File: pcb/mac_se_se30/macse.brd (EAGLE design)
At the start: 52 x 24 mm, 8 parts, among them J1 ATX24RH

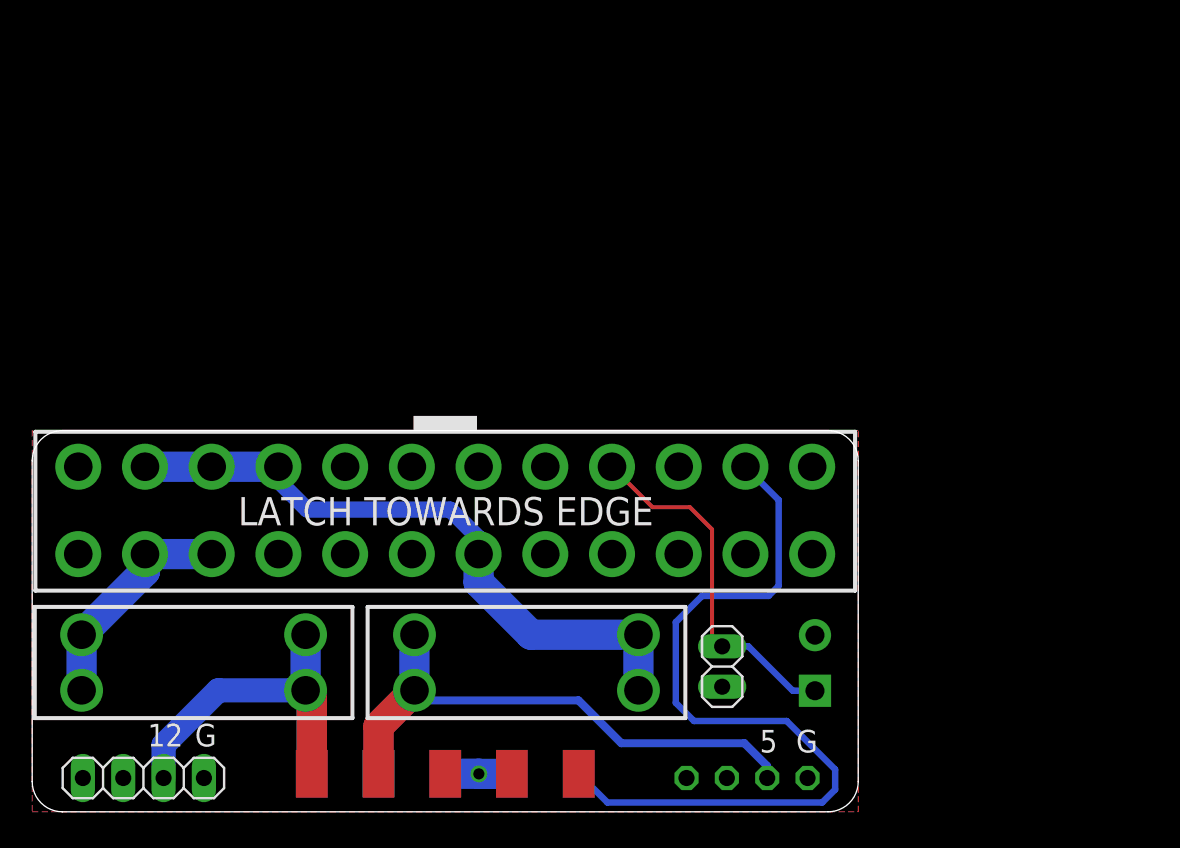
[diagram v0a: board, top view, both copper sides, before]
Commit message: updating mac SE atx adaptor
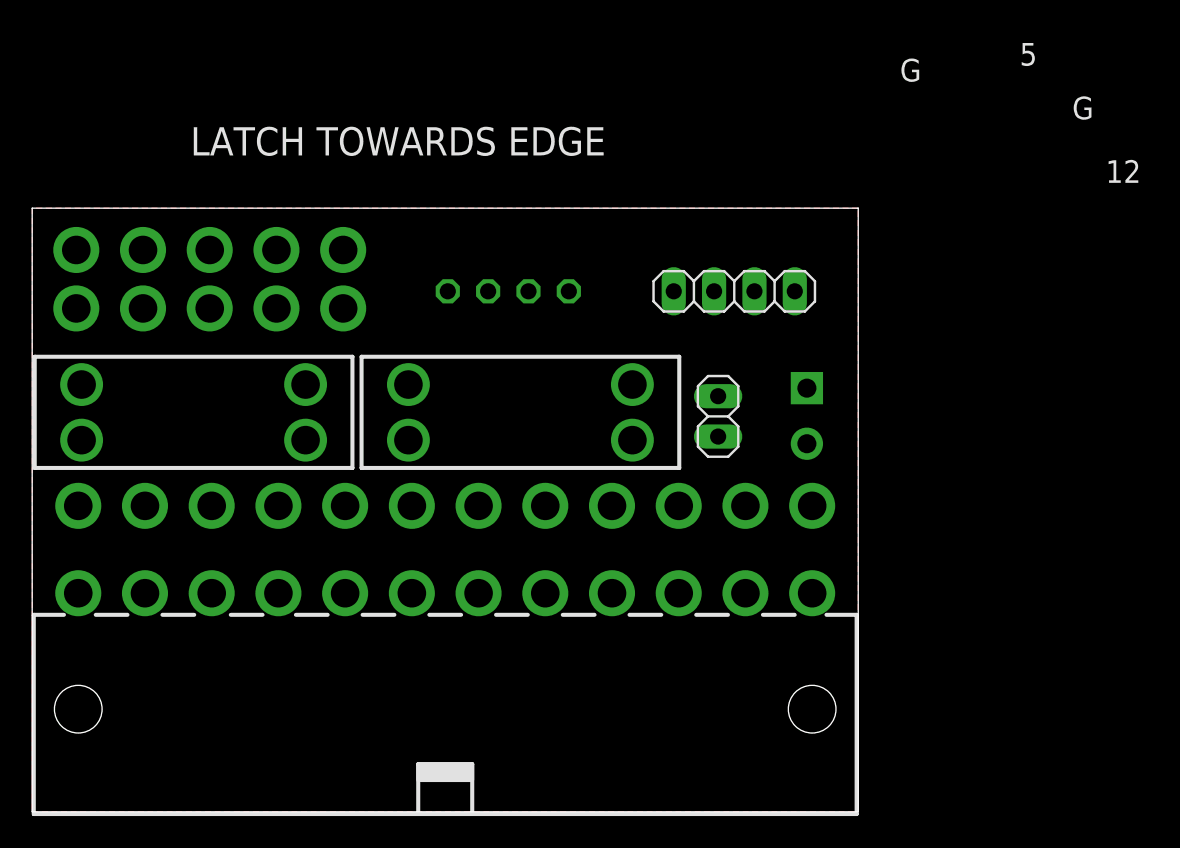
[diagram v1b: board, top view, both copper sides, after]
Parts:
- removed J1: ATX24RH, atx4vc:ATX24_STRAIGHT
- added J2: ATX24RH, SparkFun-Connectors:ATX24_RIGHT_ANGLE
- U$1: device atx4vc:MACSE_10P -> atx4vc:MACSE_10P_STRAIGHT
- moved JP1 48.2 mm to (44.2, 32.8), turned to 180 degrees
- moved U$1 34.5 mm to (11.2, 33.5), flipped to the top, turned to 0 degrees
- moved JP4 34.1 mm to (32.5, 32.8)
- moved J7 19.1 mm to (48.8, 26.7), turned to 270 degrees
- moved U$8 15.8 mm to (30.7, 25.1), turned to 180 degrees
- moved JP2 15.8 mm to (43.2, 24.9), turned to 90 degrees
- moved U$2 15.7 mm to (10.2, 25.1), turned to 180 degrees
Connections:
- net +12V: now also U$1.10, U$1.5; no longer U$1.P$10, U$1.P$5
- net +5V: now also U$1.4, U$1.9; no longer U$1.P$4, U$1.P$9
- net -12V: now also J2.14, U$1.6; no longer J1.14, U$1.P$6
- net GND: now also J2.15, J2.17, J2.18, J2.19, J2.24, J2.3, J2.5, J2.7, U$1.1, U$1.2, U$1.3, U$1.7, U$1.8; no longer J1.15, J1.17, J1.18, J1.19, J1.24, J1.3, J1.5, J1.7, U$1.P$1, U$1.P$2, U$1.P$3, U$1.P$7, U$1.P$8
- net N$5: now also J2.16; no longer J1.16
- net N$6: now also J2.21, J2.22, J2.23, J2.6; no longer J1.21, J1.22, J1.23, J1.6
- net N$8: now also J2.10, J2.11; no longer J1.10, J1.11
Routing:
- net -12V: track 51.1 -> 0.00 mm
- net N$6: track 41.1 -> 0.00 mm
- net +5V: track 40.8 -> 0.00 mm
- net +12V: track 26.8 -> 0.00 mm
- net N$5: track 22.6 -> 0.00 mm
- net N$8: track 14.4 -> 0.00 mm
- net GND: track 4.21 -> 0.00 mm, vias 1 -> 0
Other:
- board size 52 x 24 mm -> 52 x 38 mm

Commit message: updated mac SE pcb
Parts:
- removed JP4: (no value), adafruit_changed:1X06
- added JP3: (no value), atx_power_control:1X04
- added TP1: PTR1PAD1-20Y, testpad:P1-20Y
- J2: device SparkFun-Connectors:ATX24_RIGHT_ANGLE -> macse:ATX24_RIGHT_ANGLE
- moved U$2 20.6 mm to (30.7, 24.9)
- moved U$8 20.6 mm to (10.2, 24.9), turned to 0 degrees
- moved JP1 1.02 mm to (44.2, 33.8)
- moved U$1 0.38 mm to (11.2, 33.1)
- moved JP2 0.25 mm to (42.9, 24.9)
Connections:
- net +5V: now also JP3.3; no longer JP4.3
- net GND: now also JP3.4, TP1.TP; no longer JP4.4
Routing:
- net N$8: track 0.00 -> 73.5 mm
- net +12V: track 0.00 -> 70.9 mm
- net N$6: track 0.00 -> 65.6 mm
- net -12V: track 0.00 -> 58.6 mm
- net +5V: track 0.00 -> 40.3 mm
- net N$5: track 0.00 -> 15.3 mm
- net GND: track 0.00 -> 10.9 mm
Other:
- outline, holes or cut-outs redrawn
- board text added: "FUSE 5A MAX"
- board text added: "GND"
- board text added: "NOTCH TOWARDS EDGE"
- board text added: "PT1 dekuNukem Nov 2022"
- board text added: "PWR SW"
- board text removed: "LATCH TOWARDS EDGE"
- board text removed: "PT0 dekuNukem Nov 2022"

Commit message: finishing touches
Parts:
- added C1, C2: (no value), capacitor-wima:C5B2.5
- moved JP3 2.29 mm to (27.7, 33.8)
- moved JP1 1.27 mm to (45.5, 33.8)
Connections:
- net +12V: now also C1.1, C2.1
- net GND: now also C1.2, C2.2
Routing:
- net +12V: track 70.9 -> 72.6 mm
- net +5V: track 40.3 -> 38.8 mm
- net -12V: track 58.6 -> 59.6 mm
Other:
- board text added: "+"

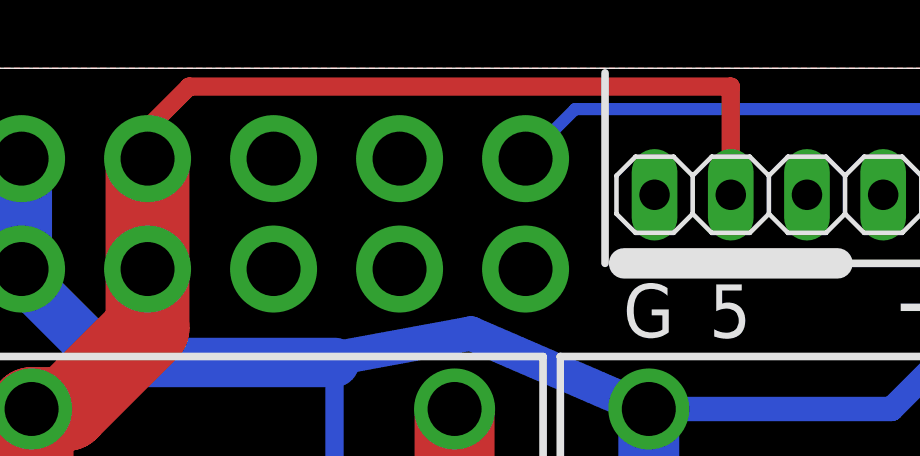
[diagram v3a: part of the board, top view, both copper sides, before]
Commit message: updated switch footprint
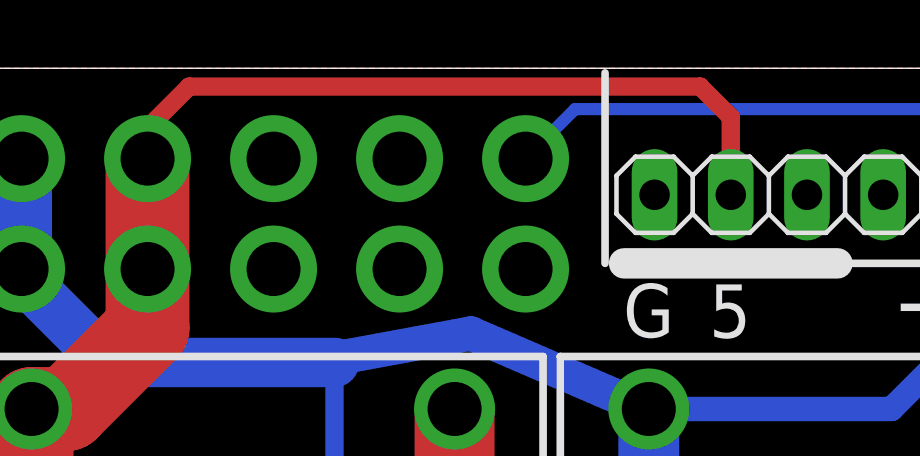
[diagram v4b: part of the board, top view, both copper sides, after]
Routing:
- net +5V: track 38.8 -> 38.2 mm
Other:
- board text added: "PD1 dekuNukem Nov 2022"
- board text removed: "PT1 dekuNukem Nov 2022"
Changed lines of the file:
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@@
 <text x="26.393" y="29.905" size="1.778" layer="25" align="center">5</text>
 <text x="26.003" y="9.567" size="1.9304" layer="26" distance="35" rot="MR0" align="center">Macintosh SE ATX Adaptor</text>
-<text x="26.051" y="6.886" size="1.4224" layer="26" distance="30" rot="MR0" align="center">PT1 dekuNukem Nov 2022</text>
+<text x="26.051" y="6.886" size="1.4224" layer="26" distance="30" rot="MR0" align="center">PD1 dekuNukem Nov 2022</text>
 <wire x1="22.225" y1="37.846" x2="22.225" y2="31.496" width="0.254" layer="21"/>
 <wire x1="22.86" y1="31.496" x2="29.972" y2="31.496" width="1.016" layer="21"/>
@@
 <wire x1="8.3618" y1="37.3888" x2="6.976" y2="36.003" width="0.6096" layer="1"/>
 <wire x1="6.976" y1="34.987" x2="6.976" y2="36.003" width="0.6096" layer="1"/>
-<wire x1="8.3618" y1="37.3888" x2="26.416" y2="37.3888" width="0.6096" layer="1"/>
+<wire x1="8.3618" y1="37.3888" x2="25.4" y2="37.3888" width="0.6096" layer="1"/>
 <contactref element="JP3" pad="3"/>
-<wire x1="26.416" y1="37.3888" x2="26.416" y2="33.782" width="0.6096" layer="1"/>
+<wire x1="25.4" y1="37.3888" x2="26.416" y2="36.3728" width="0.6096" layer="1"/>
+<wire x1="26.416" y1="36.3728" x2="26.416" y2="33.782" width="0.6096" layer="1"/>
 </signal>
 <signal name="-12V">

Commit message: updated se board
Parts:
- moved U$1 0.25 mm to (11.2, 33.4)
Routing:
- net -12V: track 59.6 -> 48.9 mm
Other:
- board size 52 x 38 mm -> 51 x 38 mm
- board text added: "PD2 dekuNukem Dec 2022"
- board text removed: "PD1 dekuNukem Nov 2022"
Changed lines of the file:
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@@
 <board>
 <plain>
-<wire x1="0" y1="36.095" x2="0" y2="1.905" width="0" layer="20"/>
-<wire x1="0" y1="1.905" x2="1.905" y2="0" width="0" layer="20" curve="90"/>
-<wire x1="1.905" y1="0" x2="50.095" y2="0" width="0" layer="20"/>
-<wire x1="50.095" y1="0" x2="52" y2="1.905" width="0" layer="20" curve="90"/>
-<wire x1="52" y1="1.905" x2="52" y2="36.095" width="0" layer="20"/>
-<wire x1="52" y1="36.095" x2="50.095" y2="38" width="0" layer="20" curve="90"/>
-<wire x1="50.095" y1="38" x2="1.905" y2="38" width="0" layer="20"/>
-<wire x1="1.905" y1="38" x2="0" y2="36.095" width="0" layer="20" curve="90"/>
+<wire x1="0" y1="35.46" x2="0" y2="2.54" width="0" layer="20"/>
+<wire x1="0" y1="2.54" x2="2.54" y2="0" width="0" layer="20" curve="90"/>
+<wire x1="2.54" y1="0" x2="48.46" y2="0" width="0" layer="20"/>
+<wire x1="48.46" y1="0" x2="51" y2="2.54" width="0" layer="20" curve="90"/>
+<wire x1="51" y1="2.54" x2="51" y2="35.46" width="0" layer="20"/>
+<wire x1="51" y1="35.46" x2="48.46" y2="38" width="0" layer="20" curve="90"/>
+<wire x1="48.46" y1="38" x2="2.54" y2="38" width="0" layer="20"/>
+<wire x1="2.54" y1="38" x2="0" y2="35.46" width="0" layer="20" curve="90"/>
 <text x="26.02" y="3.504" size="1.6764" layer="26" distance="35" rot="MR0" align="center">Instructions: atx4vc.com</text>
 <text x="23.679" y="29.921" size="1.778" layer="25" align="center">G</text>
@@
 <text x="26.393" y="29.905" size="1.778" layer="25" align="center">5</text>
 <text x="26.003" y="9.567" size="1.9304" layer="26" distance="35" rot="MR0" align="center">Macintosh SE ATX Adaptor</text>
-<text x="26.051" y="6.886" size="1.4224" layer="26" distance="30" rot="MR0" align="center">PD1 dekuNukem Nov 2022</text>
+<text x="26.051" y="6.886" size="1.4224" layer="26" distance="30" rot="MR0" align="center">PD2 dekuNukem Dec 2022</text>
 <wire x1="22.225" y1="37.846" x2="22.225" y2="31.496" width="0.254" layer="21"/>
 <wire x1="22.86" y1="31.496" x2="29.972" y2="31.496" width="1.016" layer="21"/>
@@
 TOWARDS
 EDGE</text>
-<text x="49.092" y="3.48" size="1.778" layer="26" rot="MR180" align="center">GND</text>
+<text x="47.32" y="2.61" size="1.778" layer="26" rot="MR90" align="center">GND</text>
 <text x="32.925" y="30.184" size="2.1844" layer="25" distance="35" align="center">+</text>
 <text x="40.799" y="30.184" size="2.1844" layer="26" distance="35" rot="MR0" align="center">+</text>
@@
 <attribute name="VALUE" x="46.101" y="22.352" size="1.27" layer="27" rot="R90"/>
 </element>
-<element name="U$1" library="atx4vc" package="MACSE_10P_STRAIGHT" value="MACSE" x="11.176" y="33.147" smashed="yes"/>
+<element name="U$1" library="atx4vc" package="MACSE_10P_STRAIGHT" value="MACSE" x="11.176" y="33.401" smashed="yes"/>
 <element name="JP1" library="atx_power_control" package="1X04" value="" x="45.466" y="33.782" smashed="yes" rot="R180">
 <attribute name="POPULARITY" value="9" x="45.466" y="33.782" size="1.778" layer="27" rot="R180" display="off"/>
@@
 <signal name="GND">
 <polygon width="0.1524" layer="1" isolate="0.508">
-<vertex x="52" y="38"/>
+<vertex x="51" y="38"/>
 <vertex x="0" y="38"/>
 <vertex x="0" y="11.938"/>
-<vertex x="52" y="11.938"/>
+<vertex x="51" y="11.938"/>
 </polygon>
 <contactref element="J7" pad="2"/>
@@
 <wire x1="3.11" y1="23.142" x2="3.11" y2="26.642" width="2.794" layer="1"/>
 <wire x1="3.11" y1="26.642" x2="4.29" y2="26.642" width="2.794" layer="1"/>
-<wire x1="6.976" y1="29.328" x2="6.976" y2="31.307" width="2.794" layer="1"/>
+<wire x1="6.976" y1="29.328" x2="6.976" y2="31.561" width="2.794" layer="1"/>
 <wire x1="4.29" y1="26.642" x2="6.976" y2="29.328" width="2.794" layer="1"/>
-<wire x1="6.976" y1="31.307" x2="6.976" y2="34.987" width="2.794" layer="1"/>
-<wire x1="8.3618" y1="37.3888" x2="6.976" y2="36.003" width="0.6096" layer="1"/>
-<wire x1="6.976" y1="34.987" x2="6.976" y2="36.003" width="0.6096" layer="1"/>
-<wire x1="8.3618" y1="37.3888" x2="25.4" y2="37.3888" width="0.6096" layer="1"/>
+<wire x1="6.976" y1="31.561" x2="6.976" y2="35.241" width="2.794" layer="1"/>
+<wire x1="7.93" y1="37.465" x2="6.976" y2="36.511" width="0.508" layer="1"/>
+<wire x1="6.976" y1="35.241" x2="6.976" y2="36.511" width="0.508" layer="1"/>
+<wire x1="7.93" y1="37.465" x2="25.3238" y2="37.465" width="0.508" layer="1"/>
 <contactref element="JP3" pad="3"/>
-<wire x1="25.4" y1="37.3888" x2="26.416" y2="36.3728" width="0.6096" layer="1"/>
-<wire x1="26.416" y1="36.3728" x2="26.416" y2="33.782" width="0.6096" layer="1"/>
+<wire x1="25.3238" y1="37.465" x2="26.416" y2="36.3728" width="0.508" layer="1"/>
+<wire x1="26.416" y1="36.3728" x2="26.416" y2="33.782" width="0.508" layer="1"/>
 </signal>
 <signal name="-12V">
 <contactref element="U$1" pad="6"/>
 <contactref element="J2" pad="14"/>
-<wire x1="44.9" y1="19.26" x2="42.57" y2="21.59" width="0.4064" layer="16"/>
-<wire x1="41.656" y1="21.59" x2="40.386" y2="22.86" width="0.4064" layer="16"/>
-<wire x1="42.57" y1="21.59" x2="41.656" y2="21.59" width="0.4064" layer="16"/>
-<wire x1="50.23" y1="36.638" x2="51.054" y2="35.814" width="0.4064" layer="16"/>
-<wire x1="51.054" y1="35.814" x2="51.054" y2="31.242" width="0.4064" layer="16"/>
-<wire x1="50.23" y1="36.638" x2="21.227" y2="36.638" width="0.4064" layer="16"/>
-<wire x1="19.576" y1="34.987" x2="21.227" y2="36.638" width="0.4064" layer="16"/>
-<wire x1="49.53" y1="29.718" x2="51.054" y2="31.242" width="0.4064" layer="16"/>
-<wire x1="40.386" y1="26.924" x2="41.656" y2="28.194" width="0.4064" layer="16"/>
-<wire x1="41.656" y1="28.194" x2="45.466" y2="28.194" width="0.4064" layer="16"/>
-<wire x1="46.99" y1="29.718" x2="49.53" y2="29.718" width="0.4064" layer="16"/>
-<wire x1="40.386" y1="22.86" x2="40.386" y2="26.924" width="0.4064" layer="16"/>
-<wire x1="45.466" y1="28.194" x2="46.99" y2="29.718" width="0.4064" layer="16"/>
+<wire x1="44.9" y1="19.26" x2="42.57" y2="21.59" width="0.3556" layer="16"/>
+<wire x1="41.656" y1="21.59" x2="40.386" y2="22.86" width="0.3556" layer="16"/>
+<wire x1="42.57" y1="21.59" x2="41.656" y2="21.59" width="0.3556" layer="16"/>
+<wire x1="20.973" y1="36.638" x2="19.576" y2="35.241" width="0.3556" layer="16"/>
+<wire x1="40.386" y1="26.924" x2="41.656" y2="28.194" width="0.3556" layer="16"/>
+<wire x1="40.386" y1="22.86" x2="40.386" y2="26.924" width="0.3556" layer="16"/>
+<wire x1="41.656" y1="28.194" x2="43.18" y2="28.194" width="0.3556" layer="16"/>
+<wire x1="43.18" y1="28.194" x2="45.466" y2="30.48" width="0.3556" layer="16"/>
+<wire x1="45.466" y1="30.48" x2="45.466" y2="36.068" width="0.3556" layer="16"/>
+<wire x1="44.896" y1="36.638" x2="20.973" y2="36.638" width="0.3556" layer="16"/>
+<wire x1="45.466" y1="36.068" x2="44.896" y2="36.638" width="0.3556" layer="16"/>
 </signal>
 <signal name="N$6">
@@
 <contactref element="JP1" pad="3"/>
 <wire x1="5.635" y1="28.194" x2="2.776" y2="31.053" width="1.651" layer="16"/>
-<wire x1="2.776" y1="31.053" x2="2.776" y2="31.307" width="1.524" layer="16"/>
+<wire x1="2.776" y1="31.053" x2="2.776" y2="31.561" width="1.524" layer="16"/>
 <wire x1="13.208" y1="28.194" x2="5.635" y2="28.194" width="1.651" layer="16"/>
-<wire x1="2.776" y1="31.307" x2="2.776" y2="34.987" width="2.032" layer="16"/>
+<wire x1="2.776" y1="31.561" x2="2.776" y2="35.241" width="2.032" layer="16"/>
 <wire x1="23.684" y1="23.142" x2="23.684" y2="26.642" width="2.032" layer="16"/>
 <wire x1="23.684" y1="23.142" x2="20.7204875" y2="23.142" width="0.6096" layer="16"/>
